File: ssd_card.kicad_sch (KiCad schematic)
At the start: 1 part, among them J1 SmartCard_ISO7816

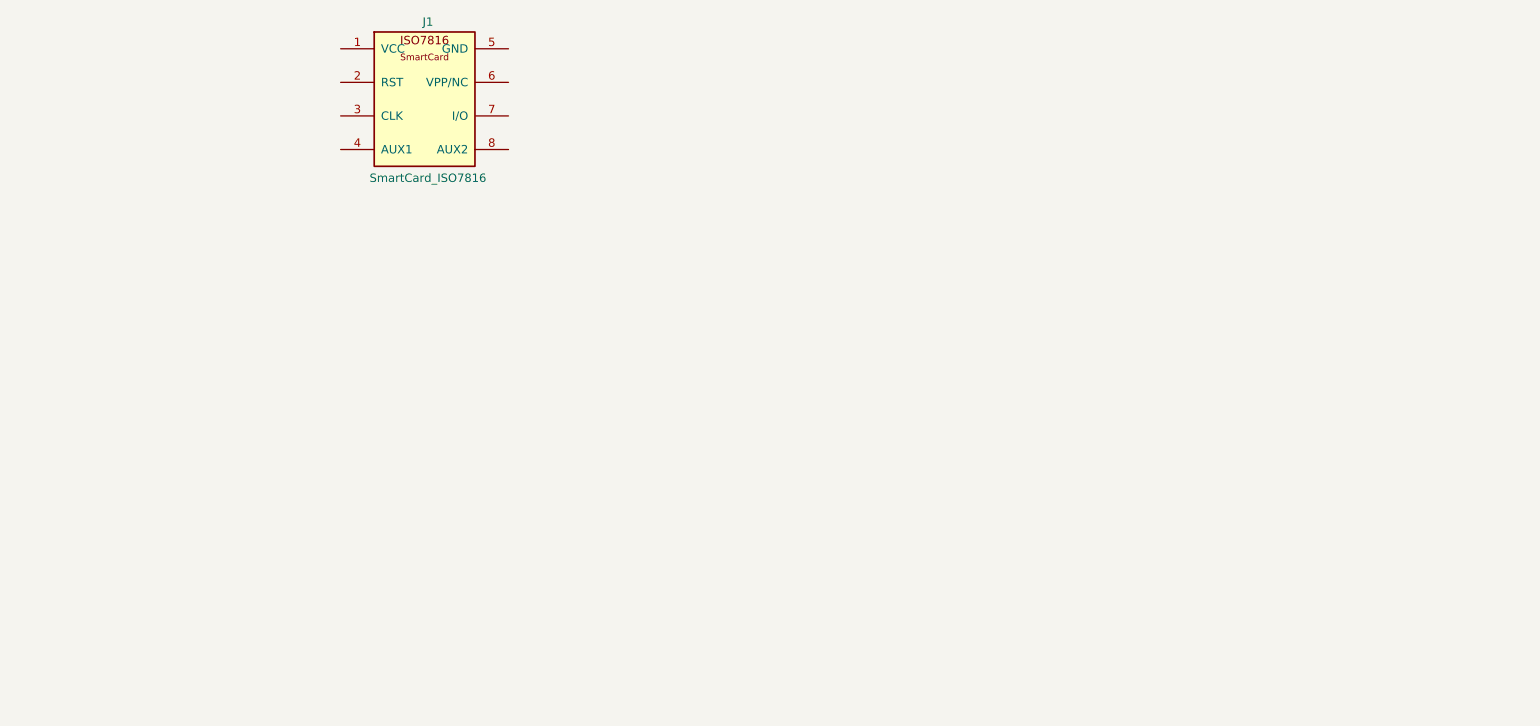
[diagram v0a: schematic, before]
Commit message: feat: STM32 start schematic
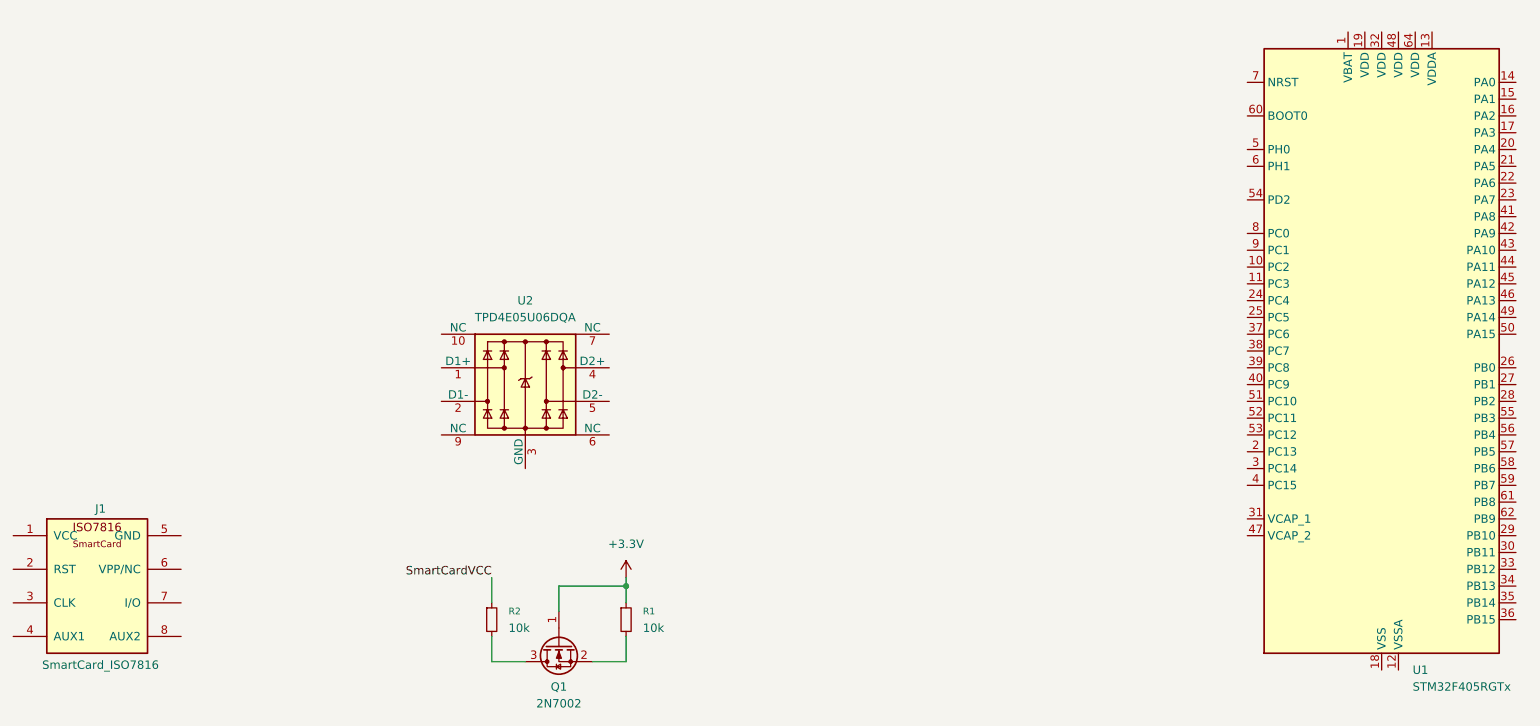
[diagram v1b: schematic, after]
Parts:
- added Q1: 2N7002, Package_TO_SOT_SMD:SOT-23, symbol Transistor_FET:2N7002
- added R1, R2: 10k, symbol Device:R_Small
- added U1: STM32F405RGTx, Package_QFP:LQFP-64_10x10mm_P0.5mm, symbol MCU_ST_STM32F4:STM32F405RGTx
- added U2: TPD4E05U06DQA, Package_SON:USON-10_2.5x1.0mm_P0.5mm, symbol Power_Protection:TPD4E05U06DQA
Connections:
- new net: Q1.2 (S), R1.2
- new net: U2.3 (GND), U2.8 (GND)
- new net: Q1.3 (D), R2.2
- new net: U1.18 (VSS), U1.63 (VSS)
- new net +3.3V: Q1.1 (G), R1.1
- new net SmartCardVCC: R2.1
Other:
- moved on the sheet: J1

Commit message: feat: Documentation
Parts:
- removed U2: TPD4E05U06DQA, Package_SON:USON-10_2.5x1.0mm_P0.5mm, symbol Power_Protection:TPD4E05U06DQA
- added R3, R4, R6: 220, symbol Device:R_Small
- added R5: 100R, symbol Device:R_Small
- added R7: 100k, symbol Device:R_Small
- added U2, U3: SN74LVC2T45DCUR, Package_SO:VSSOP-8_2.3x2mm_P0.5mm, symbol Logic_LevelTranslator:SN74LVC2T45DCUR
- R1, R2: value 10k -> 100k
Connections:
- net SmartCardVCC is gone; now on net STM32_CARD_VCC_SENSE: R2.1
- net +3.3V: now also U2.8 (VCCB), U3.8 (VCCB); no longer Q1.1 (G), R1.1
- net SC_VCC: now reaches J1.1 (VCC)
- net SC_VCC: now also R1.1, U2.1 (VCCA), U2.5 (DIR), U3.1 (VCCA), U3.5 (DIR)
- net SC_RST: now reaches J1.2 (RST)
- net SC_RST: now also R3.1
- net SC_CLK: now reaches J1.3 (CLK)
- net SC_CLK: now also R4.1
- net SC_AUX1: now reaches J1.4 (AUX1)
- net GND: now reaches J1.5 (GND)
- net GND: now also Q1.2 (S), R2.2, R7.2, U2.4 (GND), U3.2 (A1), U3.4 (GND)
- net SC_VPP: now reaches J1.6 (VPP/NC)
- net SC_IO: now reaches J1.7 (I/O)
- net SC_IO: now also Q1.3 (D), R6.1
- net SC_AUX2: now reaches J1.8 (AUX2)
- net STM32_CARD_VCC_SENSE: now reaches R1.2
- net STM32_CARD_VCC_SENSE: now also U1.14 (PA0); no longer Q1.2 (S)
- net STM32_CARD_RST: now reaches U1.26 (PB0)
- net STM32_CARD_RST: now also U2.7 (B1)
- net STM32_CARD_CLK: now reaches U1.41 (PA8)
- net STM32_CARD_CLK: now also U2.6 (B2)
- net STM32_CARD_IO_DRV: now reaches U1.42 (PA9)
- net STM32_CARD_IO_DRV: now also R5.1
- net STM32_CARD_IO_SENSE: now reaches U1.43 (PA10)
- net STM32_CARD_IO_SENSE: now also U3.6 (B2)
- new net: R4.2, U2.3 (A2)
- new net: Q1.1 (G), R5.2, R7.1
- new net: R3.2, U2.2 (A1)
- new net: R6.2, U3.3 (A2)
- no-connect marks 0 -> 1
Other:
- moved on the sheet: J1, U1

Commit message: Add HRO USB-C receptacle footprint
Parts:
- added C1, C16, C17, C18, C2, C20, C21, C3, C4, C5: 100n, Capacitor_SMD:C_0603_1608Metric, symbol Device:C_Small
- added C10, C9: 2.2uF, Capacitor_SMD:C_0603_1608Metric, symbol Device:C_Small
- added C11, C14, C15, C19, C22, C23: 10uF, Capacitor_SMD:C_0603_1608Metric, symbol Device:C_Small
- added C6: 0.1u, Capacitor_SMD:C_0603_1608Metric, symbol Device:C_Small
- added C7, C8: 20pF, Capacitor_SMD:C_0603_1608Metric, symbol Device:C_Small
- added D1: DS, LED_SMD:LED_0603_1608Metric, symbol Device:LED_Small
- added D2: DE, LED_SMD:LED_0603_1608Metric, symbol Device:LED_Small
- added D7: B, LED_SMD:LED_0603_1608Metric, symbol Device:LED_Small
- added FB1, FB3, FB4: FB, Inductor_SMD:L_0805_2012Metric, symbol Device:FerriteBead_Small
- added J2: SWD_TagConnect_TC2030, Connector:Tag-Connect_TC2030-IDC-NL_2x03_P1.27mm_Vertical, symbol Connector:Conn_ARM_SWD_TagConnect_TC2030-NL
- added JP1: SJ_ESP_BOOT, Jumper:SolderJumper-2_P1.3mm_Open_RoundedPad1.0x1.5mm, symbol Jumper:SolderJumper_2_Open
- added L1: 4.7uH, Inductor_SMD:L_0805_2012Metric, symbol Device:L_Small
- added P2, P3: USB_C_Plug_USB2.0, USB_C_HRO:USB_C_Receptacle_HRO_TYPE-C-31-M-12, symbol Connector:USB_C_Plug_USB2.0
- added Q2, Q3: BSS138, Package_TO_SOT_SMD:SOT-23, symbol Transistor_FET:BSS138
- added R10, R11, R14, R8: 10K, Resistor_SMD:R_0603_1608Metric, symbol Device:R_Small
- added R12, R15: 5.1k, Resistor_SMD:R_0603_1608Metric, symbol Device:R_Small
- added R13, R9: 300R, Resistor_SMD:R_0603_1608Metric, symbol Device:R_Small
- added R20, R21: 1k, Resistor_SMD:R_0603_1608Metric, symbol Device:R_Small
- added R22, R23: 100K, Resistor_SMD:R_0603_1608Metric, symbol Device:R_Small
- added SW2: STM_NRST, Button_Switch_SMD:SW_SPST_B3U-1000P, symbol Switch:SW_Push
- added SW3: STM_BOOT0_SW, Button_Switch_SMD:SW_SPDT_PCM12, symbol Switch:SW_SPDT
- added SW4: ESP32_BOOT_SW, Button_Switch_SMD:SW_SPDT_PCM12, symbol Switch:SW_SPDT
- added SW7: STM_SB1, Button_Switch_SMD:SW_SPST_B3U-1000P, symbol Switch:SW_Push
- added SW8: STM_SB2, Button_Switch_SMD:SW_SPST_B3U-1000P, symbol Switch:SW_Push
- added U5: ESP32-WROOM-32, RF_Module:ESP32-WROOM-32, symbol RF_Module:ESP32-WROOM-32
- added U6: CH340C, Package_SO:SOIC-16_3.9x9.9mm_P1.27mm, symbol Interface_USB:CH340C
- added U7: AP63203WU, Package_TO_SOT_SMD:TSOT-23-6, symbol Regulator_Switching:AP63203WU
- added Y1: 25Mhz, symbol Device:Crystal_GND24_Small
- R1, R2, R3, R4, R5, R6, R7: footprint (none) -> Resistor_SMD:R_0603_1608Metric
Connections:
- net +3.3V: now also U1.1 (VBAT), U1.19 (VDD), U1.32 (VDD), U1.48 (VDD), U1.64 (VDD), C1.1, C11.1, C17.1, C2.1, C21.2, C22.1, C23.1, C3.1, C4.1, C5.1, FB1.1, J2.1 (VCC), L1.2, R11.1, R8.1, SW3.3 (C), SW4.3 (C), SW7.1, SW8.1, U5.2 (VDD), U6.16 (VCC), U7.1 (FB)
- net GND: now also U1.12 (VSSA), U1.18 (VSS), U1.63 (VSS), C1.2, C10.2, C11.2, C14.2, C15.2, C16.2, C17.2, C18.2, C19.2, C2.2, C21.1, C22.2, C23.2, C3.2, C4.2, C5.2, C6.2, C7.2, C8.2, C9.2, D1.1 (K), D2.1 (K), D7.1 (K), J2.5 (GND), P2.A1 (GND), P2.A12 (GND), P2.B1 (GND), P2.B12 (GND), P3.A1 (GND), P3.A12 (GND), P3.B1 (GND), P3.B12 (GND), R12.2, R15.2, R22.2, R23.2, SW2.2, SW3.1 (A), SW4.1 (A), U5.1 (GND), U5.15 (GND), U5.38 (GND), U5.39 (GND), U6.1 (GND), U7.4 (GND), Y1.2 (G), Y1.4 (G)
- net at U1.13 (VDDA): now also FB1.2
- net STM32_LED_STATUS: now reaches U1.2 (PC13)
- net STM32_LED_STATUS: now also R20.1
- net STM32_ESP_EN: now reaches U1.20 (PA4)
- net STM32_ESP_EN: now also C18.1, R11.2, U5.3 (EN)
- net STM32_ESP_SPI_SCK: now reaches U1.21 (PA5)
- net STM32_ESP_SPI_SCK: now also U5.30 (IO18)
- net STM32_ESP_SPI_MISO: now reaches U1.22 (PA6)
- net STM32_ESP_SPI_MISO: now also U5.31 (IO19)
- net STM32_ESP_SPI_MOSI: now reaches U1.23 (PA7)
- net STM32_ESP_SPI_MOSI: now also U5.37 (IO23)
- net STM32_ESP_SPI_CS: now reaches U1.24 (PC4)
- net STM32_ESP_SPI_CS: now also U5.10 (IO25)
- net STM32_ESP_IRQ: now reaches U1.25 (PC5)
- net STM32_ESP_IRQ: now also U5.11 (IO26)
- net STM32_LED_ERROR: now reaches U1.3 (PC14)
- net STM32_LED_ERROR: now also R21.1
- net at U1.31 (VCAP_1): now also C10.1
- net STM32_SW_MODE1: now reaches U1.33 (PB12)
- net STM32_SW_MODE2: now reaches U1.34 (PB13)
- net STM32_BTN_USER1: now reaches U1.39 (PC8)
- net STM32_BTN_USER1: now also R22.1, SW7.2
- net STM32_BTN_USER2: now reaches U1.40 (PC9)
- net STM32_BTN_USER2: now also R23.1, SW8.2
- net STM32_USB_OTG_FS_DM: now reaches U1.44 (PA11)
- net STM32_USB_OTG_FS_DM: now also P3.A7 (D-)
- net STM32_USB_OTG_FS_DP: now reaches U1.45 (PA12)
- net STM32_USB_OTG_FS_DP: now also P3.A6 (D+)
- net STM32_SWDIO: now reaches U1.46 (PA13)
- net STM32_SWDIO: now also J2.2 (SWDIO)
- net at U1.47 (VCAP_2): now also C9.1
- net STM32_SWCLK: now reaches U1.49 (PA14)
- net STM32_SWCLK: now also J2.4 (SWCLK)
- net RCC_OSC_IN: now reaches U1.5 (PH0)
- net RCC_OSC_IN: now also C7.1, Y1.3
- net STM32_SWO: now reaches U1.55 (PB3)
- net STM32_SWO: now also J2.6 (SWO)
- net RCC_OSC_OUT: now reaches U1.6 (PH1)
- net RCC_OSC_OUT: now also R9.1
- net STM_BOOT0: now reaches U1.60 (BOOT0)
- net STM_BOOT0: now also R10.1
- net STM_NRST: now reaches U1.7 (NRST)
- net STM_NRST: now also C6.1, R8.2, SW2.1
- new net: FB3.1, P2.A4 (VBUS), P2.A9 (VBUS), P2.B4 (VBUS), P2.B9 (VBUS)
- new net: JP1.1 (A), R14.1
- new net: R14.2, SW4.2 (B)
- new net: P2.A5 (CC), R12.1
- new net: Q2.1 (G), Q3.3 (D), U6.13 (~{DTR})
- new net: Q2.2 (S), Q3.1 (G), U6.14 (~{RTS})
- new net: C8.1, R9.2, Y1.1
- new net: R10.2, SW3.2 (B)
- new net: C20.2, L1.1, U7.5 (SW)
- new net: D1.2 (A), R20.2
- new net: D7.2 (A), R13.2
- new net: D2.2 (A), R21.2
- new net: P3.A5 (CC), R15.1
- new net: C20.1, U7.6 (BST)
- new net: FB4.1, P3.A4 (VBUS), P3.A9 (VBUS), P3.B4 (VBUS), P3.B9 (VBUS)
- new net +5V: C14.1, C16.1, C19.1, FB3.2, FB4.2, R13.1, U7.2 (EN), U7.3 (IN)
- new net ESP32_BOOT: JP1.2 (B), Q3.2 (S), U5.25 (IO0)
- new net ESP32_EN: C15.1, Q2.3 (D)
- new net ESP32_UART_RX: U5.34 (RXD0/IO3), U6.2 (TXD)
- new net ESP32_UART_TX: U5.35 (TXD0/IO1), U6.3 (RXD)
- new net STM32_RESET: J2.3 (~{RESET})
- new net TTL_D+: P2.A6 (D+), U6.5 (UD+)
- new net TTL_D-: P2.A7 (D-), U6.6 (UD-)
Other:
- note added: "Decoupling"
- note added: "ESP32 MCU"
- note added: "ESP32 TTL"
- note added: "SmartCard Connection"
- moved on the sheet: J1, Q1, R1, R2, R3, R4, R5, R6, R7, U1, U2, U3
